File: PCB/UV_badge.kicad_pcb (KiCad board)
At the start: 2 copper layers, 28 parts, among them SW1 SW_MEC_5G, U1 LM3914N, U2 LMV321

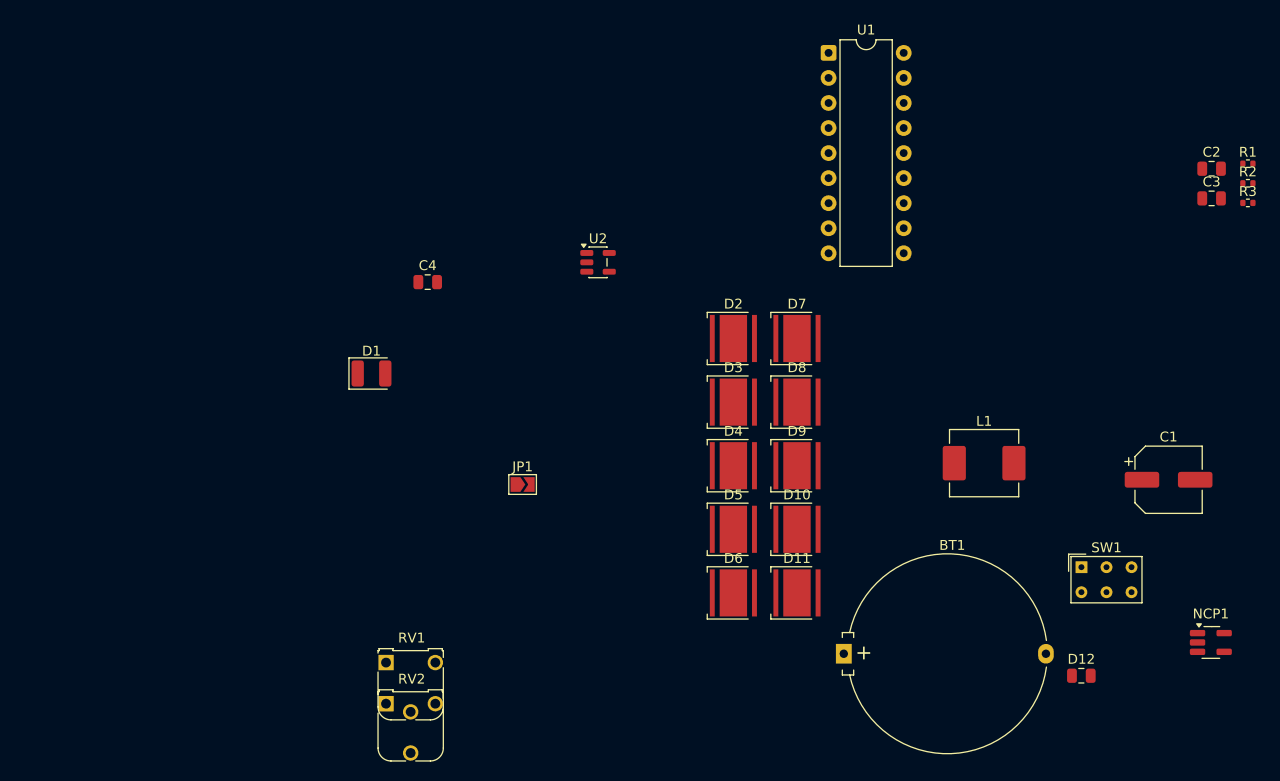
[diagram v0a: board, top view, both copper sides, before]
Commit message: update LED footprint reverse mount
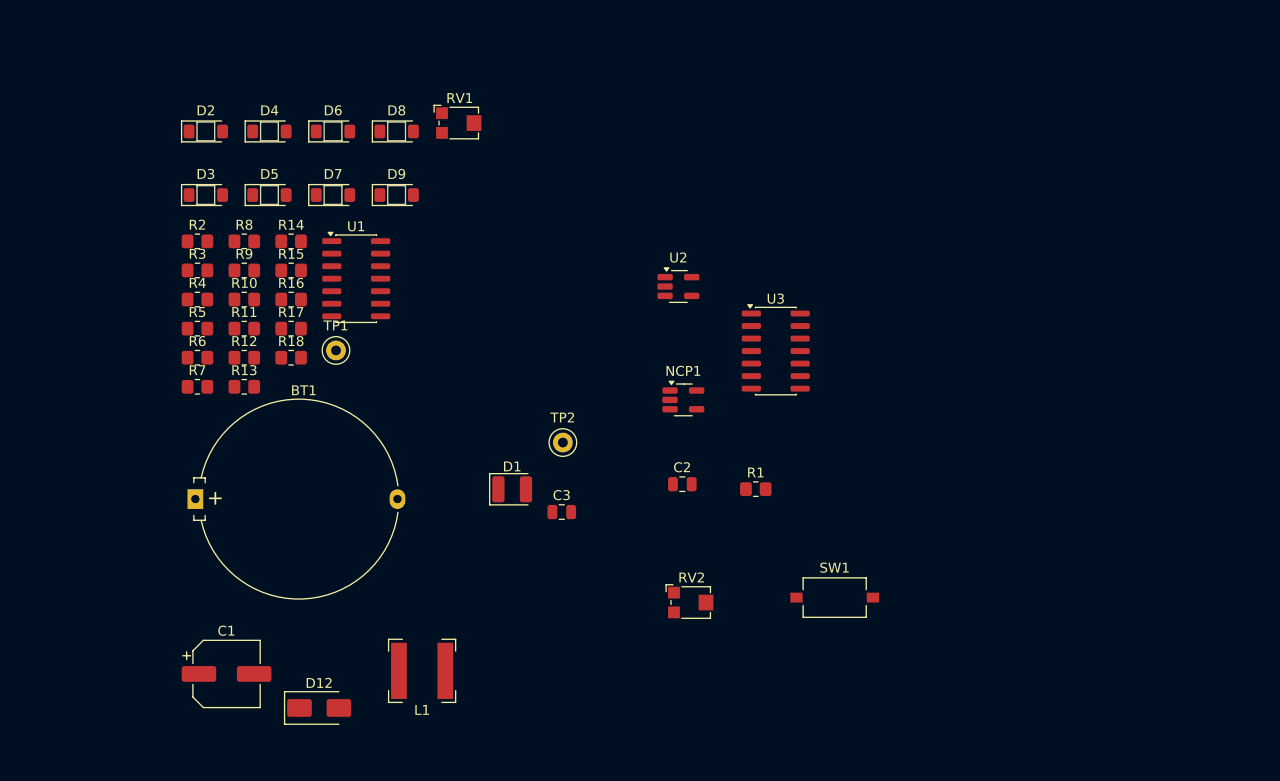
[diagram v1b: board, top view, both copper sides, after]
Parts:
- removed C4: 100n, Capacitor_SMD:C_0805_2012Metric
- removed D10, D11: LED, LED_SMD:LED_Cree-XHP50_3V_HighDensity
- removed JP1: SolderJumper, Jumper:SolderJumper-2_P1.3mm_Open_TrianglePad1.0x1.5mm
- added R10: 2k, Resistor_SMD:R_0805_2012Metric_Pad1.20x1.40mm_HandSolder, F.Cu at (115.1, 62.3)
- added R11: 470, Resistor_SMD:R_0805_2012Metric_Pad1.20x1.40mm_HandSolder, F.Cu at (115.1, 65.2)
- added R12: 470, Resistor_SMD:R_0805_2012Metric_Pad1.20x1.40mm_HandSolder, F.Cu at (115.1, 68.2)
- added R13: 470, Resistor_SMD:R_0805_2012Metric_Pad1.20x1.40mm_HandSolder, F.Cu at (115.1, 71.1)
- added R14: 470, Resistor_SMD:R_0805_2012Metric_Pad1.20x1.40mm_HandSolder, F.Cu at (119.9, 56.4)
- added R15: 470, Resistor_SMD:R_0805_2012Metric_Pad1.20x1.40mm_HandSolder, F.Cu at (119.9, 59.3)
- added R16: 470, Resistor_SMD:R_0805_2012Metric_Pad1.20x1.40mm_HandSolder, F.Cu at (119.9, 62.3)
- added R17: 470, Resistor_SMD:R_0805_2012Metric_Pad1.20x1.40mm_HandSolder, F.Cu at (119.9, 65.2)
- added R18: 470, Resistor_SMD:R_0805_2012Metric_Pad1.20x1.40mm_HandSolder, F.Cu at (119.9, 68.2)
- added R4: 2k, Resistor_SMD:R_0805_2012Metric_Pad1.20x1.40mm_HandSolder, F.Cu at (110.4, 62.3)
- added R5: 2k, Resistor_SMD:R_0805_2012Metric_Pad1.20x1.40mm_HandSolder, F.Cu at (110.4, 65.2)
- added R6: 2k, Resistor_SMD:R_0805_2012Metric_Pad1.20x1.40mm_HandSolder, F.Cu at (110.4, 68.2)
- added R7: 2k, Resistor_SMD:R_0805_2012Metric_Pad1.20x1.40mm_HandSolder, F.Cu at (110.4, 71.1)
- added R8: 2k, Resistor_SMD:R_0805_2012Metric_Pad1.20x1.40mm_HandSolder, F.Cu at (115.1, 56.4)
- added R9: 2k, Resistor_SMD:R_0805_2012Metric_Pad1.20x1.40mm_HandSolder, F.Cu at (115.1, 59.3)
- added TP1: TestPoint, TestPoint:TestPoint_Keystone_5000-5004_Miniature, F.Cu at (124.4, 67.4)
- added TP2: TestPoint, TestPoint:TestPoint_Keystone_5000-5004_Miniature, F.Cu at (147.4, 76.8)
- added U3: LM339, Package_SO:SO-14_3.9x8.65mm_P1.27mm, F.Cu at (169.0, 67.5)
- C1: footprint Capacitor_SMD:CP_Elec_6.3x7.7 -> Capacitor_SMD:CP_Elec_6.3x5.4
- D1: value D_Photo_Filled -> GUVA_S12
- D12: footprint Capacitor_SMD:C_0805_2012Metric -> Diode_SMD:D_SMA
- D2, D3, D4, D5, D6, D7, D8, D9: footprint LED_SMD:LED_Cree-XHP50_3V_HighDensity -> Library_local:LED_1206_3216Metric_ReverseMount
- L1: footprint Inductor_SMD:L_APV_APH0650 -> Inductor_SMD:L_Bourns-SRN6028
- R1: footprint Resistor_SMD:R_0402_1005Metric -> Resistor_SMD:R_0805_2012Metric_Pad1.20x1.40mm_HandSolder
- R2: value 2.2k -> 20k; footprint Resistor_SMD:R_0402_1005Metric -> Resistor_SMD:R_0805_2012Metric_Pad1.20x1.40mm_HandSolder
- R3: value 3.3k -> 4.7k; footprint Resistor_SMD:R_0402_1005Metric -> Resistor_SMD:R_0805_2012Metric_Pad1.20x1.40mm_HandSolder
- RV1: value R_Potentiometer_Trim -> 20k; footprint Potentiometer_THT:Potentiometer_Runtron_RM-065_Vertical -> Potentiometer_SMD:Potentiometer_Bourns_TC33X_Vertical
- RV2: value R_Potentiometer_Trim -> 10k; footprint Potentiometer_THT:Potentiometer_Runtron_RM-065_Vertical -> Potentiometer_SMD:Potentiometer_Bourns_TC33X_Vertical
- SW1: footprint Button_Switch_THT:SW_NKK_GW12LJP -> Button_Switch_SMD:SW_Tactile_SPST_NO_Straight_CK_PTS636Sx25SMTRLFS
- U1: value LM3914N -> LM339; footprint Package_DIP:DIP-18_W7.62mm -> Package_SO:SO-14_3.9x8.65mm_P1.27mm
- U2: footprint Package_TO_SOT_SMD:SOT-23-5 -> Package_TO_SOT_SMD:SOT-23-5_HandSoldering
- moved R3 106.8 mm to (110.4, 59.3)
- moved R2 106.7 mm to (110.4, 56.4)
- moved C1 97.5 mm to (113.3, 100.2)
- moved D12 77.4 mm to (122.7, 103.7)
- moved C3 73.2 mm to (147.3, 83.8)
- moved BT1 67.6 mm to (110.2, 82.5)
- moved C2 62.5 mm to (159.6, 81.0)
- moved D6 62.0 mm to (124.1, 45.2)
- moved L1 60.8 mm to (133.2, 99.9)
- moved R1 59.8 mm to (167.0, 81.5)
- moved NCP1 58.9 mm to (159.7, 72.5)
- moved D5 58.0 mm to (117.7, 51.7)
- moved D4 58.0 mm to (117.7, 45.2)
- moved D2 57.5 mm to (111.2, 45.2)
- moved D3 57.5 mm to (111.2, 51.7)
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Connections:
- C3 pad 1: /Amp_Sig_Out [0V-5V] -> /led_controller/signal_amp_in
- D2 pad 2: +5V -> Net-(D2-A)
- D3 pad 2: +5V -> Net-(D3-A)
- D4 pad 2: +5V -> Net-(D4-A)
- D5 pad 2: +5V -> Net-(D5-A)
- D6 pad 2: +5V -> Net-(D6-A)
- D7 pad 2: +5V -> Net-(D7-A)
- D8 pad 2: +5V -> Net-(D8-A)
- D9 pad 2: +5V -> Net-(D9-A)
- R1 pad 2: /Amp_Sig_Out [0V-5V] -> /led_controller/signal_amp_in
- R2 pad 1: Net-(U1-REFADJ) -> +5V
- R2 pad 2: GND -> Net-(R2-Pad2)
- R3 pad 1: Net-(U1-REFADJ) -> Net-(R3-Pad1)
- R3 pad 2: Net-(U1-REFOUT) -> GND
- RV1 pad 1: +5V -> Net-(R2-Pad2)
- RV1 pad 2: Net-(U1-RHI) -> Net-(U3A-+)
- RV1 pad 3: GND -> Net-(U3A-+)
- RV2 pad 1: +5V -> Net-(U1D-+)
- RV2 pad 2: Net-(U1-RLO) -> Net-(R3-Pad1)
- RV2 pad 3: GND -> Net-(R3-Pad1)
- U1 pad 1: Net-(D2-K) -> Net-(D7-K)
- U1 pad 10: Net-(D11-K) -> /led_controller/signal_amp_in
- U1 pad 12: Net-(D9-K) -> GND
- U1 pad 14: Net-(D7-K) -> Net-(D9-K)
- U1 pad 2: GND -> Net-(D6-K)
- U1 pad 4: Net-(U1-RLO) -> /led_controller/signal_amp_in
- U1 pad 5: /Amp_Sig_Out -> Net-(U1A-+)
- U1 pad 6: Net-(U1-RHI) -> /led_controller/signal_amp_in
- U1 pad 7: Net-(U1-REFOUT) -> Net-(U1B-+)
- U1 pad 8: Net-(U1-REFADJ) -> /led_controller/signal_amp_in
- U1 pad 9: Net-(JP1-B) -> Net-(U1D-+)
- U2 pad 1: GND -> /led_controller/signal_amp_in
- U2 pad 3: Net-(D1-K) -> GND
- U2 pad 4: /Amp_Sig_Out [0V-5V] -> Net-(D1-K)
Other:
- board outline added: 1.8 x 1.9 mm

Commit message: component distributions
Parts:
- removed SW1: SW_MEC_5G, Button_Switch_SMD:SW_Tactile_SPST_NO_Straight_CK_PTS636Sx25SMTRLFS
- added SW3: SW_Push, Button_Switch_SMD:SW_Push_1P1T_NO_CK_PTS125Sx73PSMTR, F.Cu at (100.5, 82.0)
- added SW4: SW_Push, Button_Switch_SMD:SW_Push_1P1T_NO_CK_PTS125Sx73PSMTR, B.Cu at (100.5, 82.0)
- moved R7 65.4 mm to (172.5, 91.5), turned to -90 degrees
- moved R6 64.9 mm to (172.5, 87.0), turned to -90 degrees
- moved R9 59.7 mm to (172.5, 76.0), turned to 90 degrees
- moved R3 59.3 mm to (150.0, 103.5)
- moved R10 58.1 mm to (172.5, 71.5), turned to -90 degrees
- moved R5 56.4 mm to (159.5, 93.0), turned to -90 degrees
- moved R4 55.7 mm to (159.5, 88.5), turned to -90 degrees
- moved D8 52.7 mm to (137.0, 97.5), turned to 180 degrees
- moved D9 52.2 mm to (137.0, 103.5), turned to 180 degrees
- moved TP1 50.4 mm to (166.0, 96.0)
- moved R8 47.4 mm to (159.5, 73.0), turned to -90 degrees
- moved R1 46.2 mm to (122.2, 70.5), turned to 180 degrees
- moved C2 43.6 mm to (121.9, 59.0), turned to 180 degrees
- moved D6 42.3 mm to (137.0, 85.5), turned to 180 degrees
- moved D7 41.9 mm to (137.0, 91.5), turned to 180 degrees
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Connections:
- D2 pad 2: Net-(D2-A) -> +5V
- D3 pad 2: Net-(D3-A) -> +5V
- D4 pad 2: Net-(D4-A) -> +5V
- D5 pad 2: Net-(D5-A) -> +5V
- D6 pad 2: Net-(D6-A) -> +5V
- D7 pad 2: Net-(D7-A) -> +5V
- D8 pad 2: Net-(D8-A) -> +5V
- D9 pad 2: Net-(D9-A) -> +5V
- NCP1 pad 3: (no net) -> unconnected-(NCP1-NC-Pad3)
- NCP1 pad 4: (no net) -> GND
- R11 pad 1: Net-(D2-A) -> Net-(R11-Pad1)
- R11 pad 2: +5V -> Net-(D2-K)
- R12 pad 1: Net-(D3-A) -> Net-(R12-Pad1)
- R12 pad 2: +5V -> Net-(D3-K)
- R13 pad 1: Net-(D4-A) -> Net-(R13-Pad1)
- R13 pad 2: +5V -> Net-(D4-K)
- R14 pad 1: Net-(D5-A) -> Net-(R14-Pad1)
- R14 pad 2: +5V -> Net-(D5-K)
- R15 pad 1: Net-(D6-A) -> Net-(R15-Pad1)
- R15 pad 2: +5V -> Net-(D6-K)
- R16 pad 1: Net-(D7-A) -> Net-(R16-Pad1)
- R16 pad 2: +5V -> Net-(D7-K)
- R17 pad 1: Net-(D8-A) -> Net-(R17-Pad1)
- R17 pad 2: +5V -> Net-(D8-K)
- R18 pad 1: Net-(D9-A) -> Net-(R18-Pad1)
- R18 pad 2: +5V -> Net-(D9-K)
- U1 pad 1: Net-(D7-K) -> Net-(R16-Pad1)
- U1 pad 13: Net-(D8-K) -> Net-(R17-Pad1)
- U1 pad 14: Net-(D9-K) -> Net-(R18-Pad1)
- U1 pad 2: Net-(D6-K) -> Net-(R15-Pad1)
- U3 pad 1: Net-(D3-K) -> Net-(R12-Pad1)
- U3 pad 13: Net-(D4-K) -> Net-(R13-Pad1)
- U3 pad 14: Net-(D5-K) -> Net-(R14-Pad1)
- U3 pad 2: Net-(D2-K) -> Net-(R11-Pad1)
